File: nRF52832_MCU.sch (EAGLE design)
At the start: 27 parts, among them J100 DEBUG_CONNECTOR, U1 NRF52832, X1 32MHz, X2 32.768kHz

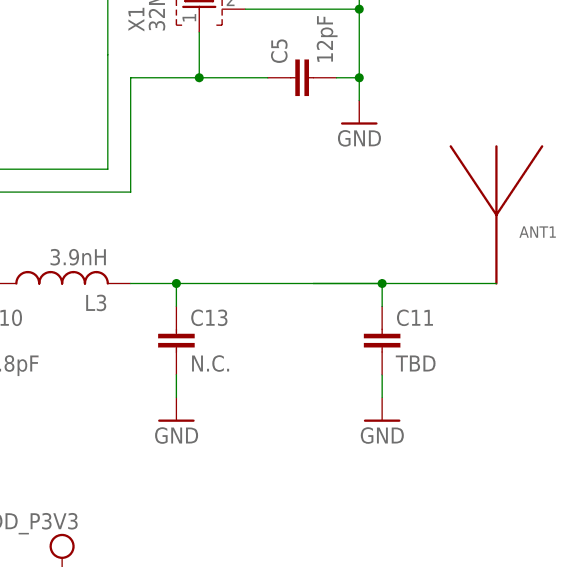
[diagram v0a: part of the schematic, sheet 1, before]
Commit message: Add missing capacitors
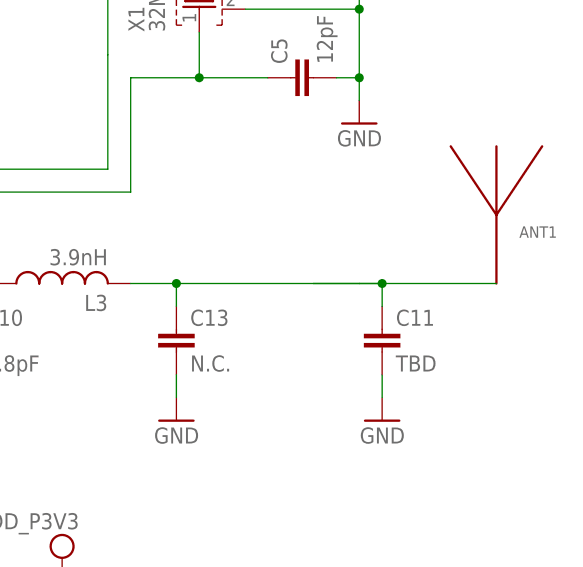
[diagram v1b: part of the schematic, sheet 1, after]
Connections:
- removed net N$1: ANT1.P$1, C11.1
- net N$5: now also ANT1.P$1, C11.1
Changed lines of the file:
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@@
-</segment>
-</net>
-<net name="N$1" class="0">
-<segment>
-<wire x1="220.98" y1="86.36" x2="228.6" y2="86.36" width="0.1524" layer="91"/>
-<wire x1="228.6" y1="86.36" x2="228.6" y2="83.82" width="0.1524" layer="91"/>
-<wire x1="228.6" y1="86.36" x2="241.3" y2="86.36" width="0.1524" layer="91"/>
-<junction x="228.6" y="86.36"/>
-<pinref part="ANT1" gate="G$1" pin="P$1"/>
-<pinref part="C11" gate="C$1" pin="1"/>
 </segment>
 </net>
@@
 <junction x="205.74" y="86.36"/>
 <wire x1="205.74" y1="86.36" x2="228.6" y2="86.36" width="0.1524" layer="91"/>
+<wire x1="220.98" y1="86.36" x2="226.06" y2="86.36" width="0.1524" layer="91"/>
+<wire x1="226.06" y1="86.36" x2="228.6" y2="86.36" width="0.1524" layer="91"/>
+<wire x1="228.6" y1="86.36" x2="228.6" y2="83.82" width="0.1524" layer="91"/>
+<junction x="228.6" y="86.36"/>
+<pinref part="ANT1" gate="G$1" pin="P$1"/>
+<pinref part="C11" gate="C$1" pin="1"/>
+<wire x1="231.14" y1="86.36" x2="241.3" y2="86.36" width="0.1524" layer="91"/>
+<wire x1="228.6" y1="86.36" x2="231.14" y2="86.36" width="0.1524" layer="91"/>
 </segment>
 </net>

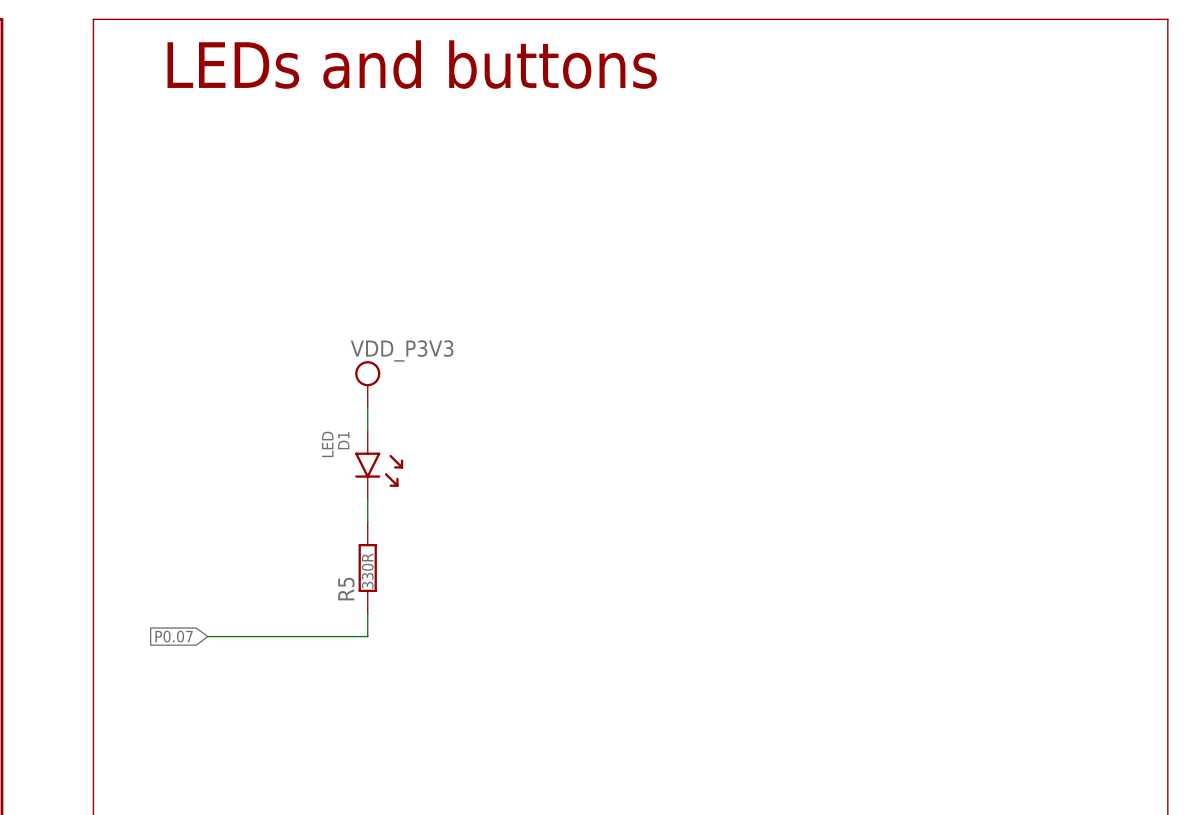
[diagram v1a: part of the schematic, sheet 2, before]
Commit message: Add additional pin connector
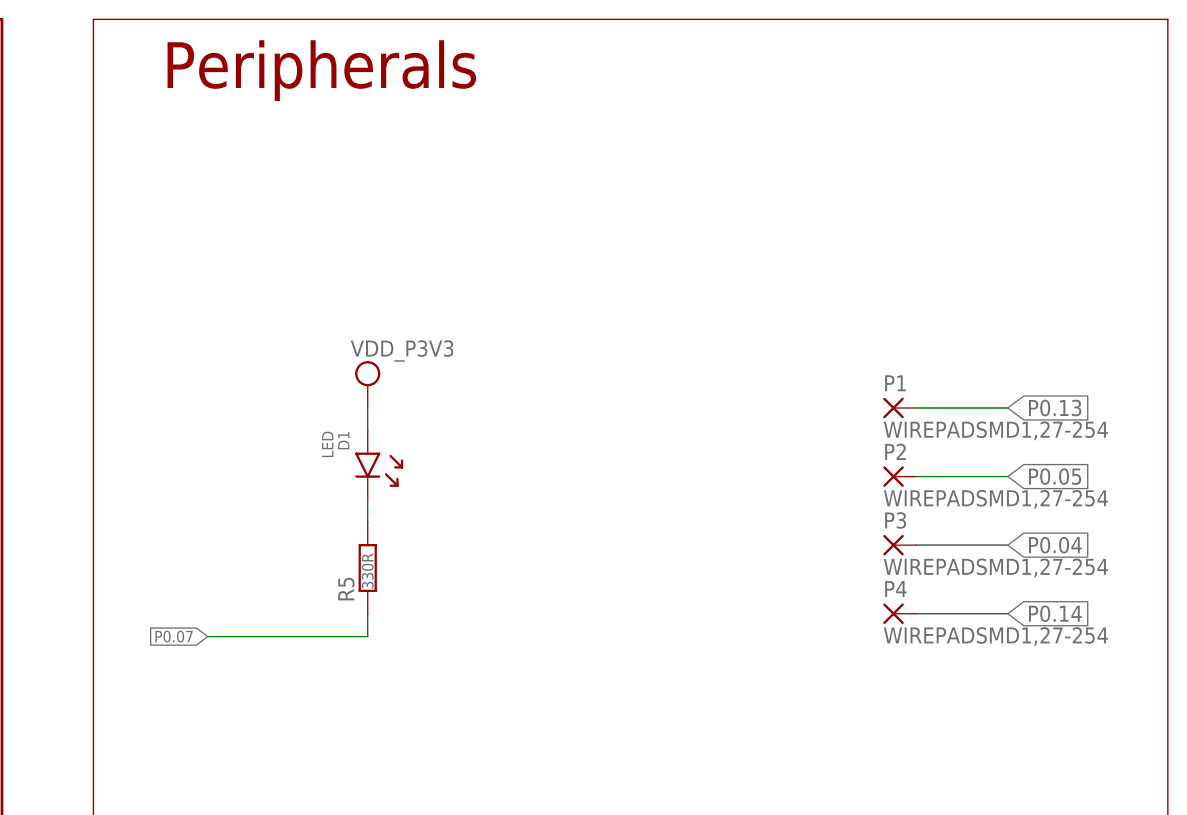
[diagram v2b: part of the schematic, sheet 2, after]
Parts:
- added P1, P2, P3, P4: WIREPADSMD1,27-254, wirepad:WIREPADSMD1,27-254
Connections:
- net P0.04: now also P3.P
- net P0.05: now also P2.P
- net P0.13: now also P1.P
- net P0.14: now also P4.P
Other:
- note added: "Peripherals"
- note removed: "LEDs and buttons"
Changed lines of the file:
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@@
 <layers>
 <layer number="1" name="Top" color="4" fill="1" visible="no" active="no"/>
+<layer number="2" name="Route2" color="1" fill="3" visible="no" active="no"/>
+<layer number="3" name="Route3" color="4" fill="3" visible="no" active="no"/>
+<layer number="4" name="Route4" color="1" fill="4" visible="no" active="no"/>
+<layer number="5" name="Route5" color="4" fill="4" visible="no" active="no"/>
+<layer number="6" name="Route6" color="1" fill="8" visible="no" active="no"/>
+<layer number="7" name="Route7" color="4" fill="8" visible="no" active="no"/>
+<layer number="8" name="Route8" color="1" fill="2" visible="no" active="no"/>
+<layer number="9" name="Route9" color="4" fill="2" visible="no" active="no"/>
+<layer number="10" name="Route10" color="1" fill="7" visible="no" active="no"/>
+<layer number="11" name="Route11" color="4" fill="7" visible="no" active="no"/>
+<layer number="12" name="Route12" color="1" fill="5" visible="no" active="no"/>
+<layer number="13" name="Route13" color="4" fill="5" visible="no" active="no"/>
+<layer number="14" name="Route14" color="1" fill="6" visible="no" active="no"/>
+<layer number="15" name="Route15" color="4" fill="6" visible="no" active="no"/>
 <layer number="16" name="Bottom" color="1" fill="1" visible="no" active="no"/>
 <layer number="17" name="Pads" color="2" fill="1" visible="no" active="no"/>
@@
 <clearance class="0" value="0.205"/>
 </class>
+<class number="1" name="New Class" width="0" drill="0">
+</class>
 </classes>
 <parts>
@@
 <part name="GND12" library="supply1" deviceset="GND" device=""/>
 <part name="GND13" library="supply1" deviceset="GND" device=""/>
+<part name="P1" library="wirepad" library_urn="urn:adsk.eagle:library:412" deviceset="WIREPAD" device="SMD1,27-254" package3d_urn="urn:adsk.eagle:package:30839/1"/>
+<part name="P2" library="wirepad" library_urn="urn:adsk.eagle:library:412" deviceset="WIREPAD" device="SMD1,27-254" package3d_urn="urn:adsk.eagle:package:30839/1"/>
+<part name="P3" library="wirepad" library_urn="urn:adsk.eagle:library:412" deviceset="WIREPAD" device="SMD1,27-254" package3d_urn="urn:adsk.eagle:package:30839/1"/>
+<part name="P4" library="wirepad" library_urn="urn:adsk.eagle:library:412" deviceset="WIREPAD" device="SMD1,27-254" package3d_urn="urn:adsk.eagle:package:30839/1"/>
 </parts>
 <sheets>
@@
 <attribute name="VALUE" x="194.945" y="59.055" size="1.778" layer="96" rot="MR0"/>
 </instance>
-<instance part="GND15" gate="1" x="193.04" y="35.56" smashed="yes">
-<attribute name="VALUE" x="190.5" y="33.02" size="1.778" layer="96"/>
+<instance part="GND15" gate="1" x="226.06" y="38.1" smashed="yes">
+<attribute name="VALUE" x="223.52" y="35.56" size="1.778" layer="96"/>
 </instance>
 <instance part="C13" gate="C$1" x="205.74" y="81.28" smashed="yes">
@@
 <pinref part="J100" gate="G$1" pin="9"/>
 <pinref part="GND15" gate="1" pin="GND"/>
-<wire x1="190.5" y1="40.64" x2="193.04" y2="40.64" width="0.1524" layer="91"/>
-<wire x1="193.04" y1="40.64" x2="193.04" y2="38.1" width="0.1524" layer="91"/>
+<wire x1="190.5" y1="40.64" x2="226.06" y2="40.64" width="0.1524" layer="91"/>
 <pinref part="J100" gate="G$1" pin="3"/>
-<wire x1="190.5" y1="48.26" x2="193.04" y2="48.26" width="0.1524" layer="91"/>
-<wire x1="193.04" y1="48.26" x2="193.04" y2="45.72" width="0.1524" layer="91"/>
-<junction x="193.04" y="40.64"/>
+<wire x1="190.5" y1="48.26" x2="226.06" y2="48.26" width="0.1524" layer="91"/>
+<junction x="226.06" y="40.64"/>
+<wire x1="226.06" y1="48.26" x2="226.06" y2="45.72" width="0.1524" layer="91"/>
 <pinref part="J100" gate="G$1" pin="5"/>
-<wire x1="193.04" y1="45.72" x2="193.04" y2="40.64" width="0.1524" layer="91"/>
-<wire x1="190.5" y1="45.72" x2="193.04" y2="45.72" width="0.1524" layer="91"/>
-<junction x="193.04" y="45.72"/>
+<wire x1="226.06" y1="45.72" x2="226.06" y2="40.64" width="0.1524" layer="91"/>
+<wire x1="190.5" y1="45.72" x2="226.06" y2="45.72" width="0.1524" layer="91"/>
+<junction x="226.06" y="45.72"/>
 </segment>
 <segment>
@@
 <net name="P0.26" class="0">
 <segment>
-<pinref part="U1" gate="U$1" pin="P0.26@38"/>
-<wire x1="132.08" y1="119.38" x2="132.08" y2="121.92" width="0.1524" layer="91"/>
 <pinref part="C16" gate="C$1" pin="1"/>
 <wire x1="167.64" y1="154.94" x2="167.64" y2="160.02" width="0.1524" layer="91"/>
 <wire x1="167.64" y1="160.02" x2="132.08" y2="160.02" width="0.1524" layer="91"/>
-<wire x1="132.08" y1="160.02" x2="132.08" y2="119.38" width="0.1524" layer="91"/>
+<pinref part="U1" gate="U$1" pin="P0.26@38"/>
+<wire x1="132.08" y1="127" x2="132.08" y2="160.02" width="0.1524" layer="91"/>
+<wire x1="132.08" y1="119.38" x2="132.08" y2="127" width="0.1524" layer="91"/>
 <junction x="132.08" y="119.38"/>
 </segment>
@@
 <label x="203.2" y="43.18" size="1.27" layer="95" xref="yes"/>
 <pinref part="J100" gate="G$1" pin="7"/>
-<wire x1="190.5" y1="43.18" x2="213.36" y2="43.18" width="0.1524" layer="91"/>
 <wire x1="203.2" y1="43.18" x2="190.5" y2="43.18" width="0.1524" layer="91"/>
-<junction x="190.5" y="43.18"/>
 </segment>
 </net>
@@
 <wire x1="10.16" y1="167.64" x2="10.16" y2="60.96" width="0.3048" layer="94"/>
 <text x="12.7" y="160.02" size="5.08" layer="94">Power sources</text>
-<text x="137.16" y="160.02" size="5.08" layer="94">LEDs and buttons</text>
+<text x="137.16" y="160.02" size="5.08" layer="94">Peripherals</text>
 <wire x1="129.54" y1="167.64" x2="248.92" y2="167.64" width="0.1524" layer="94"/>
 <wire x1="248.92" y1="167.64" x2="248.92" y2="76.2" width="0.1524" layer="94"/>
@@
 <attribute name="VALUE" x="30.48" y="116.84" size="1.778" layer="96" rot="MR0"/>
 </instance>
+<instance part="P1" gate="G$1" x="218.44" y="124.46" smashed="yes">
+<attribute name="NAME" x="217.297" y="126.3142" size="1.778" layer="95"/>
+<attribute name="VALUE" x="217.297" y="121.158" size="1.778" layer="96"/>
+</instance>
+<instance part="P2" gate="G$1" x="218.44" y="116.84" smashed="yes">
+<attribute name="NAME" x="217.297" y="118.6942" size="1.778" layer="95"/>
+<attribute name="VALUE" x="217.297" y="113.538" size="1.778" layer="96"/>
+</instance>
+<instance part="P3" gate="G$1" x="218.44" y="109.22" smashed="yes">
+<attribute name="NAME" x="217.297" y="111.0742" size="1.778" layer="95"/>
+<attribute name="VALUE" x="217.297" y="105.918" size="1.778" layer="96"/>
+</instance>
+<instance part="P4" gate="G$1" x="218.44" y="101.6" smashed="yes">
+<attribute name="NAME" x="217.297" y="103.4542" size="1.778" layer="95"/>
+<attribute name="VALUE" x="217.297" y="98.298" size="1.778" layer="96"/>
+</instance>
 </instances>
 <busses>
@@
 </segment>
 </net>
+<net name="P0.13" class="0">
+<segment>
+<wire x1="220.98" y1="124.46" x2="231.14" y2="124.46" width="0.1524" layer="91"/>
+<label x="231.14" y="124.46" size="1.778" layer="95" xref="yes"/>
+<pinref part="P1" gate="G$1" pin="P"/>
+</segment>
+</net>
+<net name="P0.05" class="0">
+<segment>
+<wire x1="220.98" y1="116.84" x2="231.14" y2="116.84" width="0.1524" layer="91"/>
+<label x="231.14" y="116.84" size="1.778" layer="95" xref="yes"/>
+<pinref part="P2" gate="G$1" pin="P"/>
+</segment>
+</net>
+<net name="P0.04" class="0">
+<segment>
+<wire x1="220.98" y1="109.22" x2="231.14" y2="109.22" width="0.1524" layer="91"/>
+<label x="231.14" y="109.22" size="1.778" layer="95" xref="yes"/>
+<pinref part="P3" gate="G$1" pin="P"/>
+</segment>
+</net>
+<net name="P0.14" class="0">
+<segment>
+<wire x1="220.98" y1="101.6" x2="231.14" y2="101.6" width="0.1524" layer="91"/>
+<label x="231.14" y="101.6" size="1.778" layer="95" xref="yes"/>
+<pinref part="P4" gate="G$1" pin="P"/>
+</segment>
+</net>
 </nets>
 </sheet>
 </sheets>
+<errors>
+</errors>
 </schematic>
 </drawing>
+<compatibility>
+<note version="8.2" severity="warning">
+Since Version 8.2, EAGLE supports online libraries. The ids
+of those online libraries will not be understood (or retained)
+with this version.
+</note>
+<note version="8.3" severity="warning">
+Since Version 8.3, EAGLE supports URNs for individual library
+assets (packages, symbols, and devices). The URNs of those assets
+will not be understood (or retained) with this version.
+</note>
+<note version="8.3" severity="warning">
+Since Version 8.3, EAGLE supports the association of 3D packages
+with devices in libraries, schematics, and board files. Those 3D
+packages will not be understood (or retained) with this version.
+</note>
+</compatibility>
 </eagle>

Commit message: Add coplanar computation
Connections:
- net GND renamed N$10
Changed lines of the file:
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@@
 </busses>
 <nets>
-<net name="GND" class="0">
+<net name="N$10" class="0">
 <segment>
 <pinref part="GND1" gate="1" pin="GND"/>
@@
 </segment>
 </net>
-<net name="GND" class="0">
+<net name="N$10" class="0">
 <segment>
 <pinref part="GND30" gate="1" pin="GND"/>
